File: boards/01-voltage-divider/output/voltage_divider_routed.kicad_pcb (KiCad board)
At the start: 2 copper layers, 30 x 25 mm, 4 parts, among them J1 Conn_01x02, J2 Conn_01x02

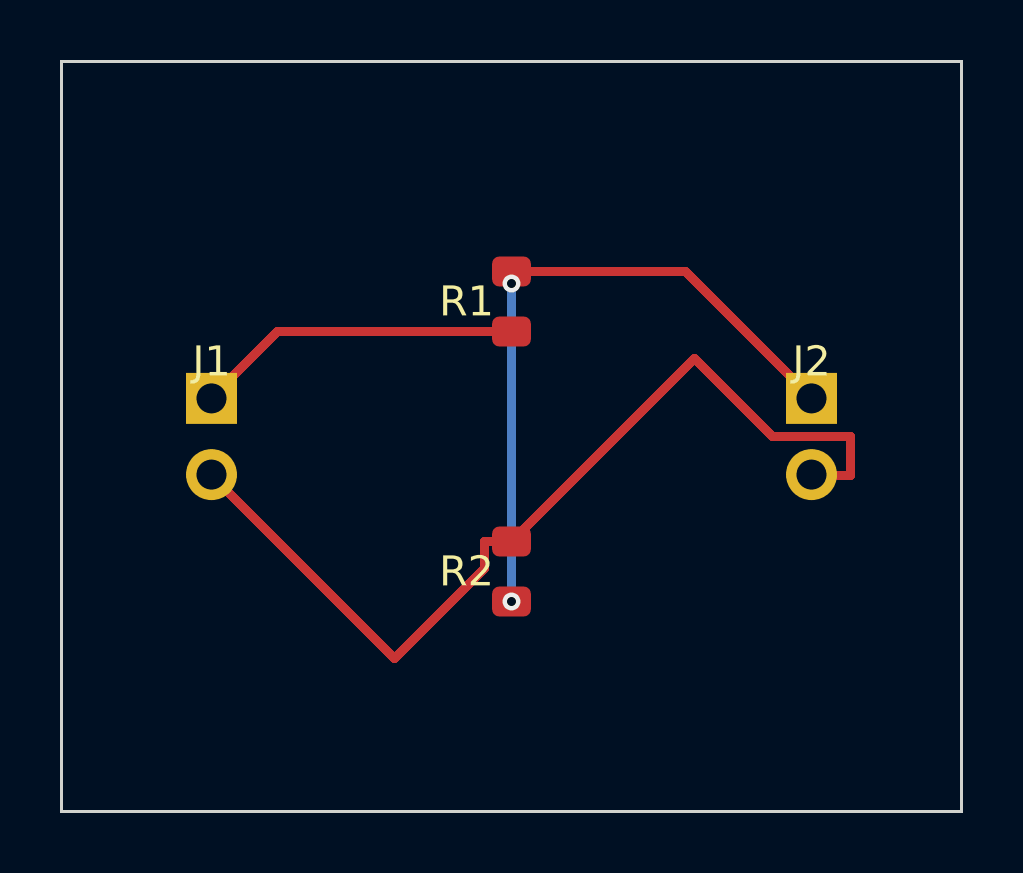
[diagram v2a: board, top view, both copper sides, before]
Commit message: fix(schematic): Remove floating wire endpoints in voltage divider
The VIN and GND power rails were extending to x=199.39mm (X_RIGHT)
but no components connected that far right. The rightmost connections
are R1 (x=110.49mm) for VIN and J2 (x=165.10mm) for GND.

Fix: Only extend rails to their rightmost actual connection points
instead of an arbitrary X_RIGHT boundary. This eliminates the
floating wire endpoints that caused ERC warnings.

Before: 2 floating_wire errors, 2 ERC warnings
After: No errors, no warnings

Closes #725

Co-Authored-By: Claude Opus 4.5 <noreply@anthropic.com>
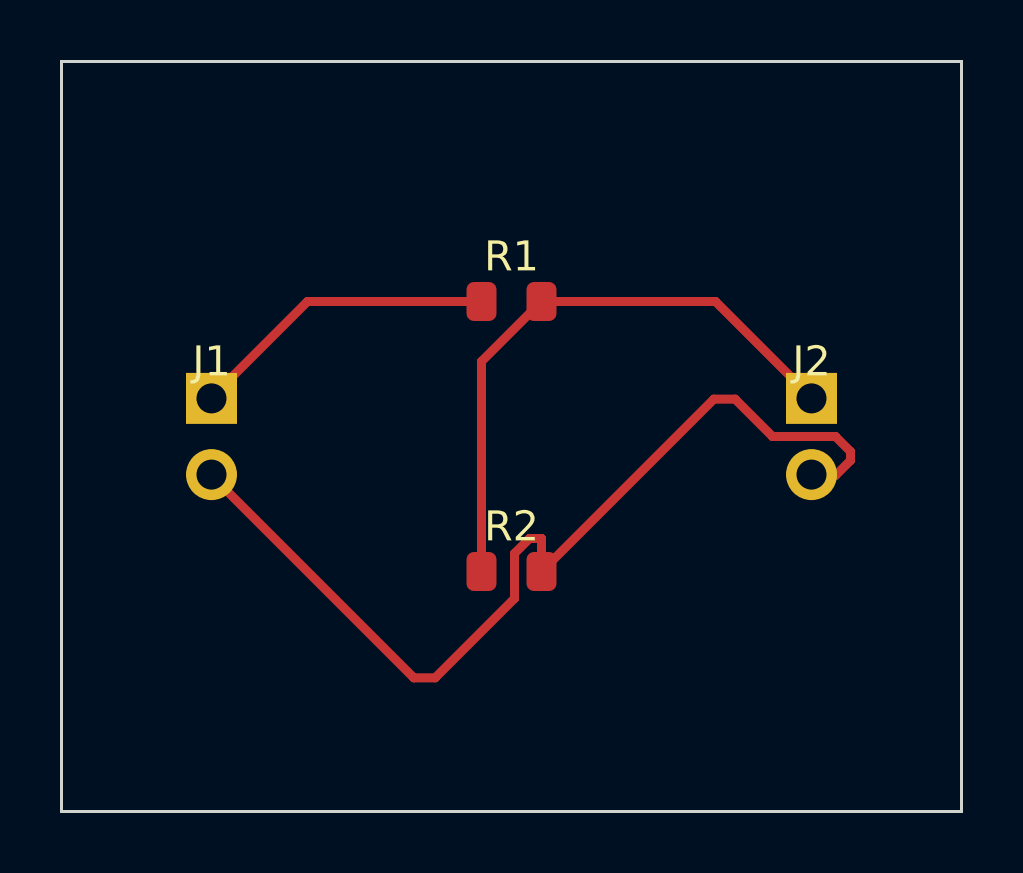
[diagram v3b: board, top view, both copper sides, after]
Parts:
- turned R1 to 0 degrees
- turned R2 to 0 degrees
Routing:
- net VOUT: track 22.8 -> 20.2 mm, vias 2 -> 0
- net VIN: track 10.9 -> 10.4 mm

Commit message: fix(footprint): use R_0805 in default profile and fix board 02 U1 footprint (#1545)
Change the default footprint selector profile to map all resistor values
to R_0805_2012Metric instead of R_0402_1005Metric, matching what the PCB
generation scripts actually place. Also fix board 02's U1 schematic
footprint from PinHeader_1x08 to DIP-8_W7.62mm to match its PCB footprint.

Regenerate output files for boards 01 and 02 to reflect corrected footprints.

Co-authored-by: Claude Opus 4.6 <noreply@anthropic.com>
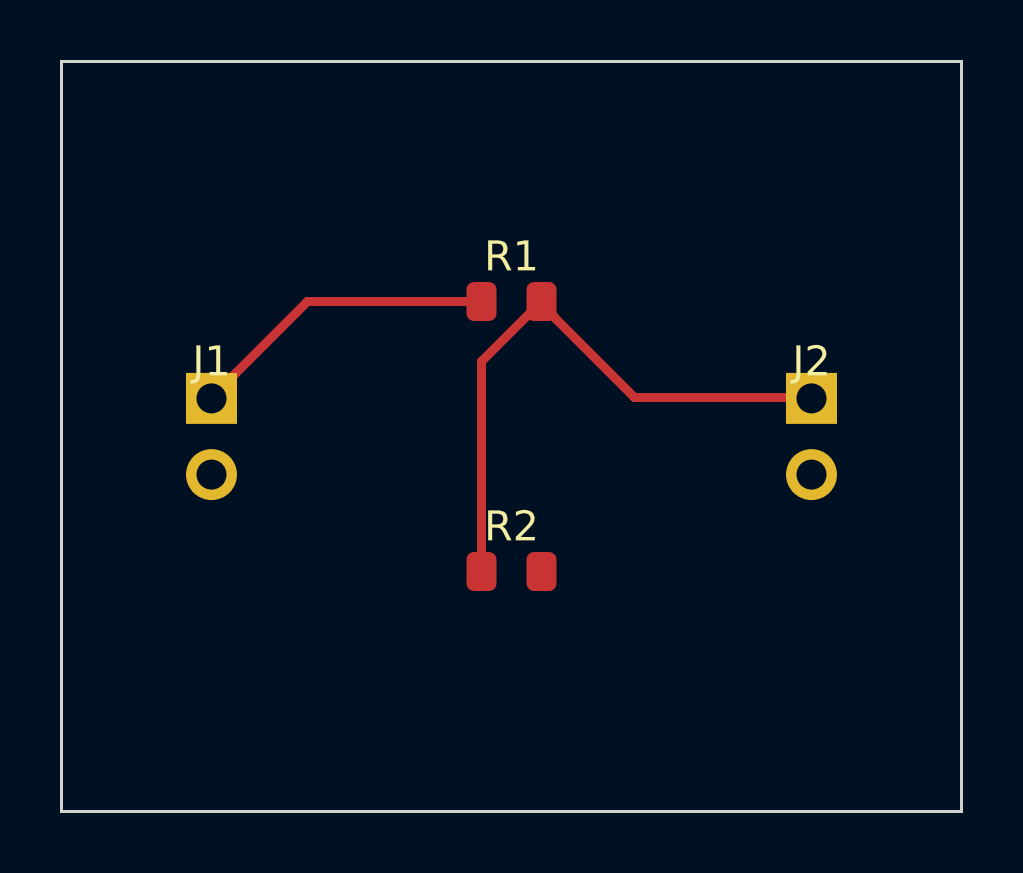
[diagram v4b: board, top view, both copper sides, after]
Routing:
- net GND: track 32.5 -> 0.00 mm
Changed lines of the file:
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@@
   )
   (segment
-		(start 116.0000 117.0000)
-		(end 121.7464 111.2536)
-		(width 0.3)
-		(layer "F.Cu")
-		(net 3)
-	)
-	(segment
-		(start 121.7464 111.2536)
-		(end 122.4536 111.2536)
-		(width 0.3)
-		(layer "F.Cu")
-		(net 3)
-	)
-	(segment
-		(start 122.4536 111.2536)
-		(end 123.7000 112.5000)
-		(width 0.3)
-		(layer "F.Cu")
-		(net 3)
-	)
-	(segment
-		(start 123.7000 112.5000)
-		(end 125.8000 112.5000)
-		(width 0.3)
-		(layer "F.Cu")
-		(net 3)
-	)
-	(segment
-		(start 125.8000 112.5000)
-		(end 126.3000 113.0000)
-		(width 0.3)
-		(layer "F.Cu")
-		(net 3)
-	)
-	(segment
-		(start 126.3000 113.0000)
-		(end 126.3000 113.3000)
-		(width 0.3)
-		(layer "F.Cu")
-		(net 3)
-	)
-	(segment
-		(start 126.3000 113.3000)
-		(end 125.8000 113.8000)
-		(width 0.3)
-		(layer "F.Cu")
-		(net 3)
-	)
-	(segment
-		(start 125.8000 113.8000)
-		(end 125.5000 113.8000)
-		(width 0.3)
-		(layer "F.Cu")
-		(net 3)
-	)
-	(segment
-		(start 125.0000 113.8000)
-		(end 125.0000 113.7700)
-		(width 0.3)
-		(layer "F.Cu")
-		(net 3)
-	)
-	(segment
-		(start 105.0000 113.7700)
-		(end 105.0000 113.8000)
-		(width 0.3)
-		(layer "F.Cu")
-		(net 3)
-	)
-	(segment
-		(start 105.0000 113.8000)
-		(end 111.7464 120.5464)
-		(width 0.3)
-		(layer "F.Cu")
-		(net 3)
-	)
-	(segment
-		(start 111.7464 120.5464)
-		(end 112.4536 120.5464)
-		(width 0.3)
-		(layer "F.Cu")
-		(net 3)
-	)
-	(segment
-		(start 112.4536 120.5464)
-		(end 115.1000 117.9000)
-		(width 0.3)
-		(layer "F.Cu")
-		(net 3)
-	)
-	(segment
-		(start 115.1000 117.9000)
-		(end 115.1000 116.4000)
-		(width 0.3)
-		(layer "F.Cu")
-		(net 3)
-	)
-	(segment
-		(start 115.1000 116.4000)
-		(end 115.6000 115.9000)
-		(width 0.3)
-		(layer "F.Cu")
-		(net 3)
-	)
-	(segment
-		(start 115.6000 115.9000)
-		(end 116.0000 115.9000)
-		(width 0.3)
-		(layer "F.Cu")
-		(net 3)
-	)
-	(segment
-		(start 116.0000 115.9000)
-		(end 116.0000 116.4000)
-		(width 0.3)
-		(layer "F.Cu")
-		(net 3)
-	)
-	(segment
-		(start 116.0000 116.4000)
-		(end 116.0000 117.0000)
-		(width 0.3)
-		(layer "F.Cu")
-		(net 3)
-	)
-	(segment
 		(start 105.0000 111.2300)
-		(end 105.0000 111.2000)
+		(end 105.8000 110.4000)
 		(width 0.3)
 		(layer "F.Cu")
@@
 	)
 	(segment
-		(start 105.0000 111.2000)
+		(start 105.8000 110.4000)
 		(end 108.2000 108.0000)
 		(width 0.3)
@@
 	(segment
 		(start 116.0000 108.0000)
-		(end 121.8000 108.0000)
+		(end 116.5000 108.6000)
 		(width 0.3)
 		(layer "F.Cu")
@@
 	)
 	(segment
-		(start 121.8000 108.0000)
-		(end 125.0000 111.2000)
+		(start 116.5000 108.6000)
+		(end 119.1000 111.2000)
 		(width 0.3)
 		(layer "F.Cu")
@@
 	)
 	(segment
-		(start 125.0000 111.2000)
+		(start 119.1000 111.2000)
+		(end 124.2000 111.2000)
+		(width 0.3)
+		(layer "F.Cu")
+		(net 2)
+	)
+	(segment
+		(start 124.2000 111.2000)
 		(end 125.0000 111.2300)
 		(width 0.3)
